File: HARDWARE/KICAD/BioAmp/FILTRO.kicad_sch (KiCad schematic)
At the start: 29 parts, among them U2 LM324, U3 LM324

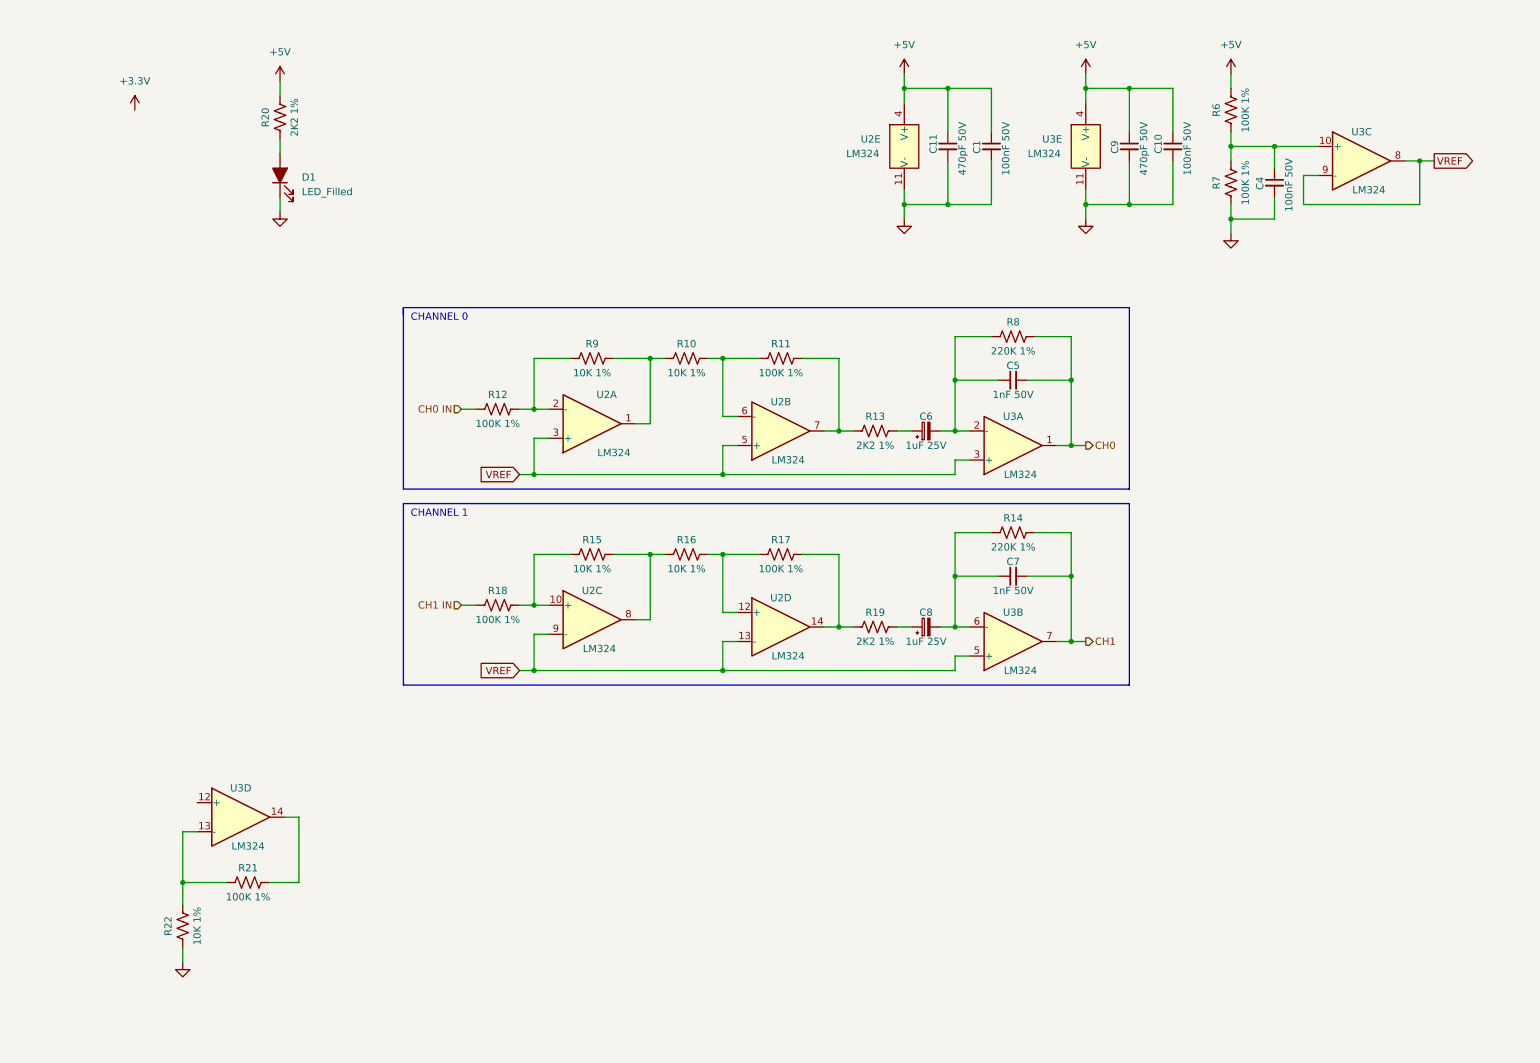
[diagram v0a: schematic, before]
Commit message: Corrigido circuito AFE (Analog Front End); adição dos ports necessários na folha principal; transferência do LED de indicação de energia para folha de fontes; adição da sugestão para novo ADC.
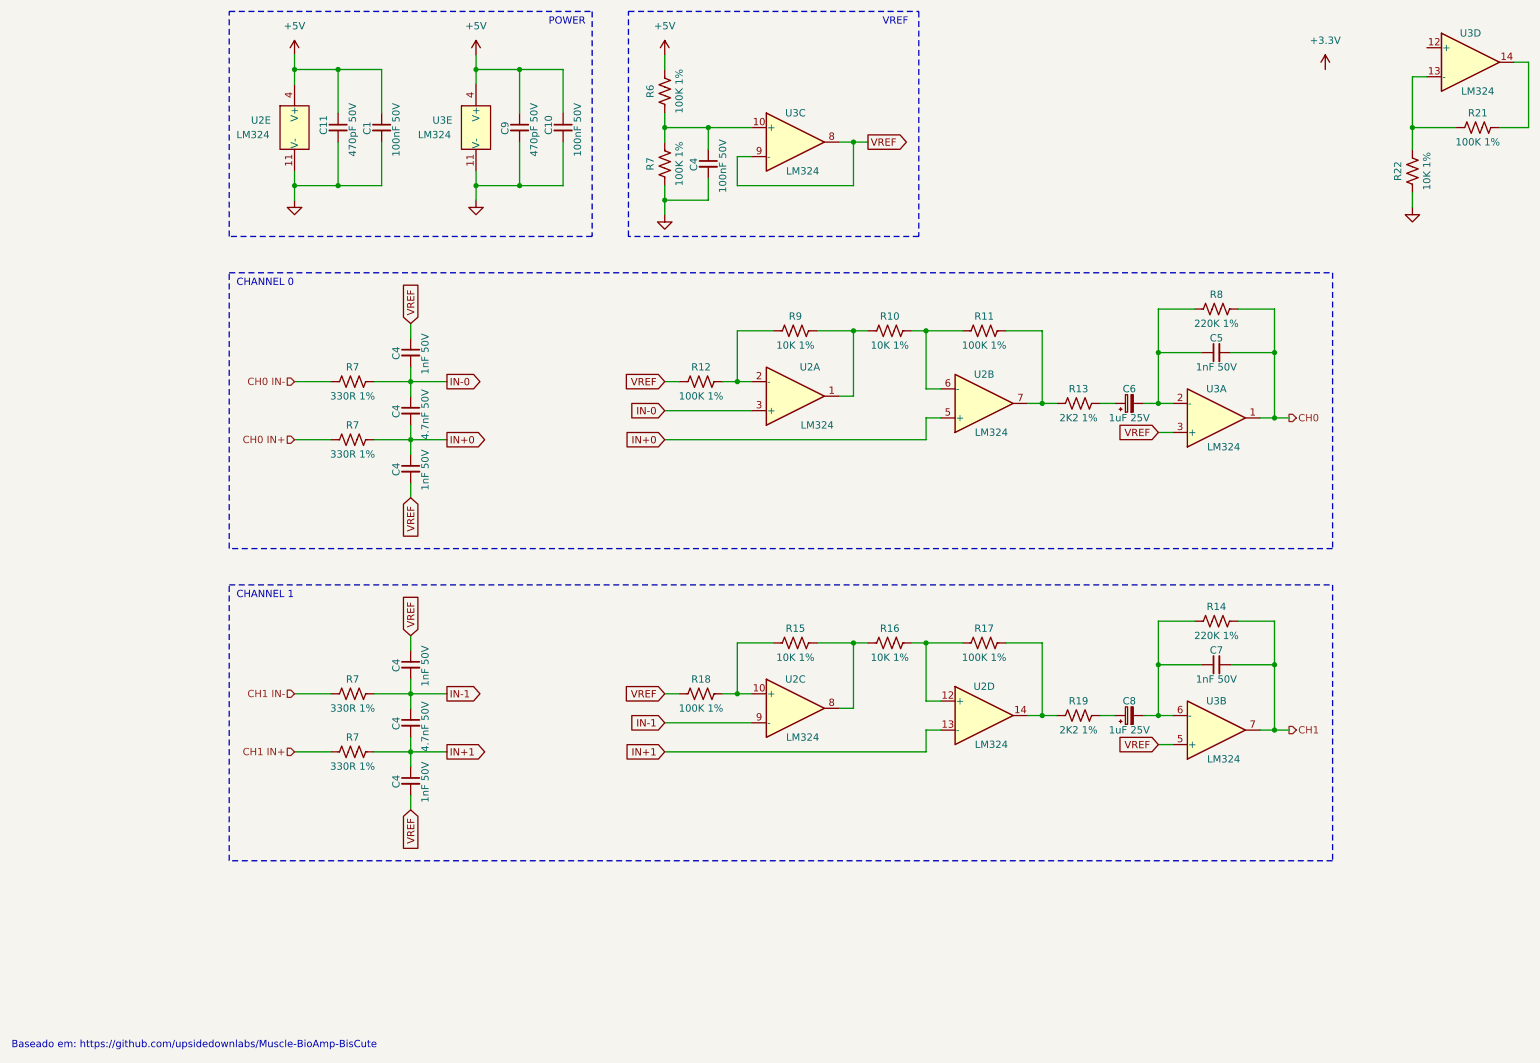
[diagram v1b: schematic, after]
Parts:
- removed D1: LED_Filled, symbol Device:LED_Filled
- removed R20: 2K2 1%, symbol Device:R_US
- added C4 (x2): 4.7nF 50V, symbol Device:C_Small
- added C4 (x4): 1nF 50V, symbol Device:C_Small
- added R7 (x4): 330R 1%, symbol Device:R_US
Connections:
- net CH0 IN is gone; now on net VREF: R12.1
- net CH1 IN is gone; now on net VREF: R18.1
- net VREF: now also C4.1, C4.1, C4.2, C4.2; no longer U2.13 (-), U2.3 (+), U2.5 (+), U2.9 (-)
- new net CH0 IN+: R7.1
- new net CH0 IN-: R7.1
- new net CH1 IN+: R7.1
- new net CH1 IN-: R7.1
- new net IN+0: C4.1, C4.2, R7.2, U2.5 (+)
- new net IN+1: C4.1, C4.2, R7.2, U2.13 (-)
- new net IN-0: C4.1, C4.2, R7.2, U2.3 (+)
- new net IN-1: C4.1, C4.2, R7.2, U2.9 (-)
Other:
- note added: "Baseado em: https://github.com/upsidedownlabs/Muscle-BioAmp-BisCute"
- note added: "POWER"
- note added: "VREF"
- moved on the sheet: C1, C10, C11, C4, C5, C6, C7, C8, C9, R10, R11, R12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
